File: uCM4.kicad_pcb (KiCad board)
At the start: 2 copper layers, 55 x 40 mm, 66 parts, among them J1 UART, J10 Conn_01x04, J11 Conn_02x06_Odd_Even, J2 Micro_SD_Card_Det, J3 I2C1, J4 USB_B_Micro, J5 DummyJ, J6 DummyJ, J7 SolderJumper_2_Open, J8 Camera 0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

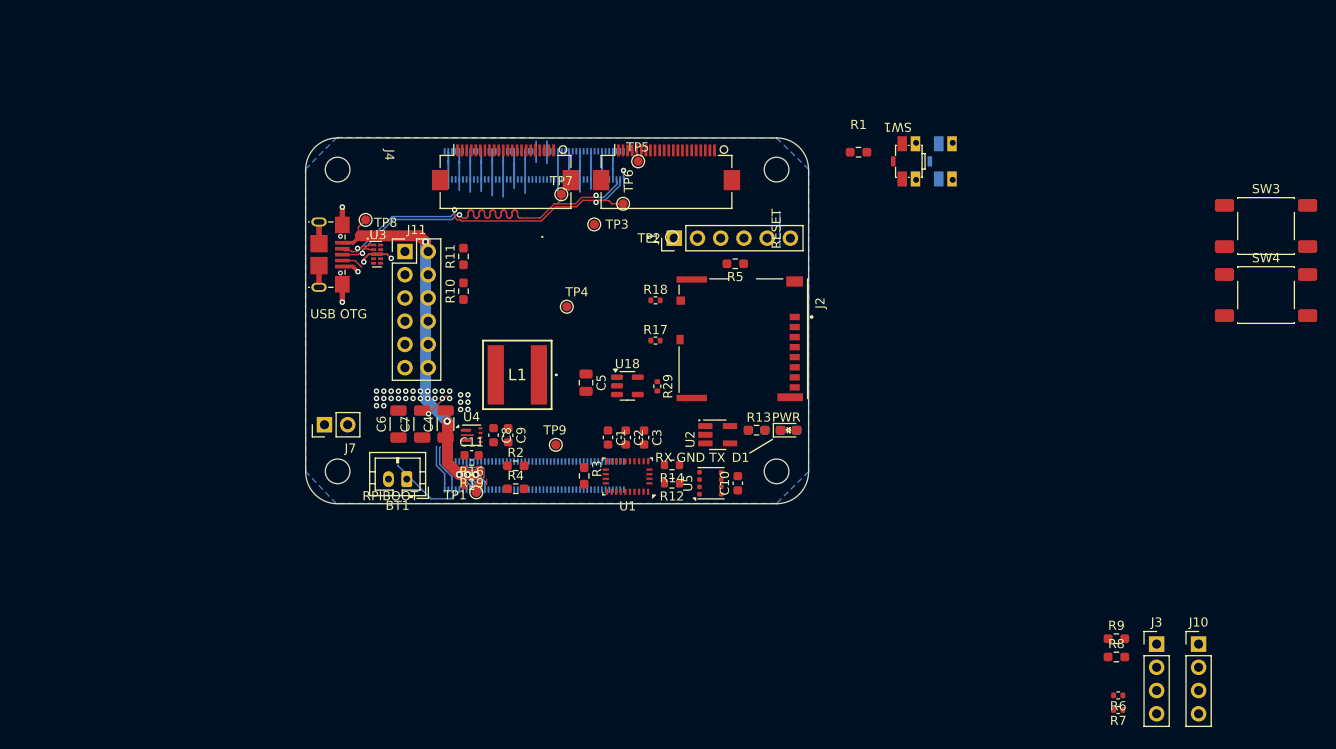
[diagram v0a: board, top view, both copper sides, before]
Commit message: Changing models & some initial routing
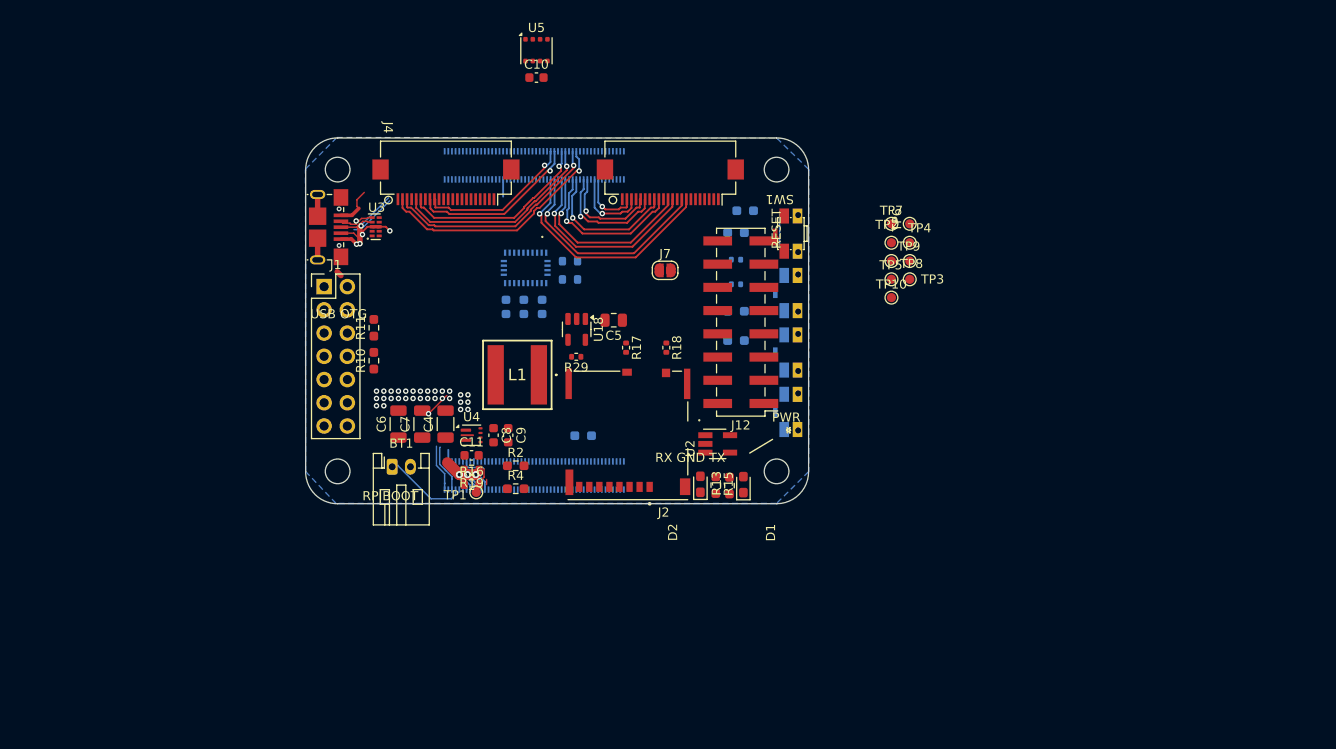
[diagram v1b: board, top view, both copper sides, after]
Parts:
- removed J10: Conn_01x04, Connector_PinHeader_2.54mm:PinHeader_1x04_P2.54mm_Vertical
- removed J11: Conn_02x06_Odd_Even, Connector_PinHeader_2.54mm:PinHeader_2x06_P2.54mm_Vertical
- removed J3: I2C1, Connector_PinHeader_2.54mm:PinHeader_1x04_P2.54mm_Vertical
- removed R5, R8, R9: 0, Resistor_SMD:R_0603_1608Metric_Pad0.98x0.95mm_HandSolder
- added J12: Conn_02x08_Odd_Even, Connector_PinHeader_2.54mm:PinHeader_2x08_P2.54mm_Vertical_SMD, F.Cu at (168.5, 105.2)
- added R20: 0, Resistor_SMD:R_0603_1608Metric_Pad0.98x0.95mm_HandSolder, B.Cu at (168.0, 107.2)
- added R21: 0, Resistor_SMD:R_0603_1608Metric_Pad0.98x0.95mm_HandSolder, B.Cu at (168.0, 95.4)
- added R22: 0, Resistor_SMD:R_0603_1608Metric_Pad0.98x0.95mm_HandSolder, B.Cu at (168.0, 104.0)
- added TP10: TestPoint, TestPoint:TestPoint_Pad_D1.0mm, F.Cu at (185.0, 102.5)
- BT1: footprint Connector_JST:JST_PH_B2B-PH-K_1x02_P2.00mm_Vertical -> Connector_JST:JST_PH_S2B-PH-K_1x02_P2.00mm_Horizontal
- C1, C2, C3, R1, R12, R14, R3, R6, R7, U1: moved to B.Cu
- D2, R15: moved to F.Cu
- J1: value UART -> Conn_02x07_Odd_Even; footprint Connector_PinHeader_2.54mm:PinHeader_1x06_P2.54mm_Vertical -> Connector_PinHeader_2.54mm:PinHeader_2x07_P2.54mm_Vertical
- J7: footprint Connector_PinHeader_2.54mm:PinHeader_1x02_P2.54mm_Vertical -> Jumper:SolderJumper-2_P1.3mm_Open_RoundedPad1.0x1.5mm
- SW3, SW4: footprint Button_Switch_SMD:SW_Push_1P1T_NO_E-Switch_TL3301NxxxxxG -> KiCAD_Randoms:PTS840_PM_SMTR_LFS; moved to B.Cu
- moved R6 63.4 mm to (168.0, 98.4), turned to 0 degrees
- moved R7 62.6 mm to (168.0, 101.0), turned to 0 degrees
- moved TP8 57.7 mm to (185.0, 98.5)
- moved SW3 55.8 mm to (174.0, 115.0), turned to -90 degrees
- moved SW4 52.0 mm to (174.0, 102.0), turned to -90 degrees
- moved U5 51.0 mm to (146.2, 75.4), turned to 0 degrees
- moved C10 49.5 mm to (146.2, 78.4), turned to 0 degrees
- moved TP9 43.6 mm to (187.0, 98.5)
- moved J7 40.9 mm to (160.2, 99.5), turned to 0 degrees
- moved J1 38.7 mm to (123.0, 101.3), turned to 0 degrees
- moved TP4 38.1 mm to (187.0, 96.5)
- moved TP7 36.2 mm to (185.0, 94.4)
- moved TP3 35.0 mm to (187.0, 100.5)
- moved TP5 30.6 mm to (185.0, 100.5)
- moved TP6 29.6 mm to (185.0, 96.5)
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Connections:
- net Net-(BT1-+) renamed /BAT_IN
- J1 pad 1: GND -> /GPS_EN_1
- J1 pad 2: /CTS0 -> /GPS_EN_2
- J1 pad 3: Net-(J1-Pin_3) -> GND
- J1 pad 4: /TXD0 -> GND
- J1 pad 5: /RXD0 -> /TXD3
- J1 pad 6: /RTS0 -> /TXD4
- R10 pad 1: Net-(J11-Pin_10) -> Net-(J1-Pin_10)
- R11 pad 2: Net-(J11-Pin_9) -> Net-(J1-Pin_9)
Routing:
- net GND: track 93.4 -> 19.5 mm, vias 21 -> 20
- net /USB_N: track 41.3 -> 4.07 mm, vias 3 -> 1
- net +5V: track 56.7 -> 24.2 mm, vias 5 -> 3
- net /USB_P: track 43.3 -> 14.2 mm, vias 3 -> 1
- net /CAM0_D0_N: track 0.00 -> 26.4 mm, vias 0 -> 1
- net /CAM1_D3_P: track 0.00 -> 25.9 mm, vias 0 -> 1
- net /CAM0_D0_P: track 0.00 -> 24.5 mm, vias 0 -> 1
- net /CAM1_D3_N: track 0.00 -> 24.2 mm, vias 0 -> 1
- net /CAM0_D1_N: track 0.00 -> 22.6 mm, vias 0 -> 1
- net /CAM1_D2_P: track 0.00 -> 21.9 mm, vias 0 -> 1
- net /CAM0_D1_P: track 0.00 -> 21.2 mm, vias 0 -> 1
- net /CAM1_D2_N: track 0.00 -> 20.3 mm, vias 0 -> 1
- net /CAM0_C_N: track 0.00 -> 18.7 mm, vias 0 -> 1
- net /CAM1_C_P: track 0.00 -> 17.6 mm, vias 0 -> 1
- net /CAM0_C_P: track 0.00 -> 17.2 mm, vias 0 -> 1
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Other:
- board text added: "#Do we need the USB"
- board text added: "Check GPS orientation. And pinout needs to change."
- board text added: "Removed keepout area. Assuming external antenna use only!"
- board text removed: "POWER"

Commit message: Rearrangements
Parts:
- removed C10: 100nF, Capacitor_SMD:C_0603_1608Metric
- removed R21, R22: 0, Resistor_SMD:R_0603_1608Metric_Pad0.98x0.95mm_HandSolder
- removed U5: BME690, Package_LGA:Bosch_LGA-8_3x3mm_P0.8mm_ClockwisePinNumbering
- added C13: 100nF, Capacitor_SMD:C_0603_1608Metric, F.Cu at (96.7, 110.5)
- added IC1: MAX17048G+, CM4:SON50P200X200X80-9N-D, F.Cu at (91.7, 111.0)
- added J10: USB_C_Receptacle, Connector_USB:USB_C_Receptacle_Amphenol_12401610E4-2A, F.Cu at (125.0, 97.1)
- added J11: SolderJumper_2_Open, Connector_PinHeader_2.54mm:PinHeader_1x02_P2.54mm_Vertical_SMD_Pin1Left, F.Cu at (105.4, 107.4)
- added J3: Conn_01x04, Connector_JST:JST_SH_BM03B-SRSS-TB_1x03-1MP_P1.00mm_Vertical, F.Cu at (92.5, 93.9)
- added R23: 0, Resistor_SMD:R_0603_1608Metric_Pad0.98x0.95mm_HandSolder, F.Cu at (96.8, 108.0)
- added R5: 0, Resistor_SMD:R_0603_1608Metric_Pad0.98x0.95mm_HandSolder, F.Cu at (96.8, 105.5)
- added R8: 5.1k, Resistor_SMD:R_0402_1005Metric, F.Cu at (110.8, 104.8)
- added R9: 5.1k, Resistor_SMD:R_0402_1005Metric, F.Cu at (110.8, 106.8)
- added U6: TP4057, Package_TO_SOT_SMD:TSOT-23-6, F.Cu at (92.1, 106.7)
- C1, C2, C3, R1, R12, R14, R20, R6, R7, U1: moved to F.Cu
- J1: footprint Connector_PinHeader_2.54mm:PinHeader_2x07_P2.54mm_Vertical -> Connector_PinHeader_2.54mm:PinHeader_2x07_P2.54mm_Vertical_SMD
- J4: value USB_B_Micro -> Conn_01x04; footprint Special:U254-05XX-4BH81 -> Connector_JST:JST_SH_BM03B-SRSS-TB_1x03-1MP_P1.00mm_Vertical
- J7: footprint Jumper:SolderJumper-2_P1.3mm_Open_RoundedPad1.0x1.5mm -> Connector_PinHeader_2.54mm:PinHeader_1x02_P2.54mm_Vertical_SMD_Pin1Left
- moved J4 28.2 mm to (97.5, 100.5), turned to 0 degrees
- moved J1 10.9 mm to (125.5, 111.9)
- moved R6 7.27 mm to (161.5, 101.7), turned to 180 degrees
- moved R7 7.21 mm to (161.4, 104.0)
- moved R20 6.84 mm to (161.3, 108.5)
- moved C3 5.18 mm to (146.8, 98.3), turned to -90 degrees
- moved C1 5.18 mm to (142.8, 98.3), turned to -90 degrees
- moved C2 5.18 mm to (144.8, 98.3), turned to -90 degrees
- moved R12 4.82 mm to (149.8, 103.3)
- moved R18 4.07 mm to (156.4, 108.8)
- moved U1 3.35 mm to (145.0, 102.6)
- moved R17 1.45 mm to (154.7, 108.7)
- moved R1 1.19 mm to (169.9, 93.8)
- moved R14 0.82 mm to (149.8, 101.3)
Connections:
- BT1 pad 1: /BAT_IN -> /BAT
- C8 pad 1: /BAT_IN -> /BOOST_IN
- C9 pad 1: /BAT_IN -> /BOOST_IN
- J12 pad 10: /SCL1 -> unconnected-(J12-Pin_10-Pad10)
- J12 pad 12: /SDA1 -> unconnected-(J12-Pin_12-Pad12)
- J12 pad 14: GND -> unconnected-(J12-Pin_14-Pad14)
- J12 pad 16: Net-(J12-Pin_16) -> unconnected-(J12-Pin_16-Pad16)
- J12 pad 2: /SCL0 -> unconnected-(J12-Pin_2-Pad2)
- J12 pad 4: /SDA0 -> unconnected-(J12-Pin_4-Pad4)
- J12 pad 6: GND -> unconnected-(J12-Pin_6-Pad6)
- J12 pad 8: Net-(J12-Pin_8) -> unconnected-(J12-Pin_8-Pad8)
- J4 pad 1: +5V -> GND
- J4 pad 2: /USB_N -> Net-(J4-Pin_2)
- J4 pad 3: /USB_P -> /SDA1
- L1 pad 1: /BAT_IN -> /BOOST_IN
- Module1 pad 101: /USB_ID -> Net-(J11-Pin_2)
- Module1 pad 41: unconnected-(Module1A-GPIO25-Pad41) -> /BAT_ALERT
- U4 pad 5: /BAT_IN -> /BOOST_IN
- U4 pad 7: /BAT_IN -> /BOOST_IN
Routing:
- net /USB_P: track 14.2 -> 0.00 mm, vias 1 -> 0
- net GND: track 19.5 -> 5.98 mm, vias 20 -> 16
- net +5V: track 24.2 -> 19.8 mm
- net /USB_N: track 4.07 -> 0.00 mm, vias 1 -> 0
- net /USB_ID: track 2.42 -> 0.00 mm
- net Net-(J1-Pin_10): vias 0 -> 2
- net /TXD4: vias 6 -> 5
- net /RXD3: vias 2 -> 1

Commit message: Changed some parts and hopeful final PCB arrangement.
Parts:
- removed J1: Conn_02x07_Odd_Even, Connector_PinHeader_2.54mm:PinHeader_2x07_P2.54mm_Vertical_SMD
- removed J3: Conn_01x04, Connector_JST:JST_SH_BM03B-SRSS-TB_1x03-1MP_P1.00mm_Vertical
- removed R11, R5: 0, Resistor_SMD:R_0603_1608Metric_Pad0.98x0.95mm_HandSolder
- removed SW4: SW_Push, KiCAD_Randoms:PTS840_PM_SMTR_LFS
- added D3: LED, LED_SMD:LED_0402_1005Metric, F.Cu at (160.1, 111.2)
- added D6: LED, LED_SMD:LED_0402_1005Metric, F.Cu at (147.1, 112.2)
- added D7: LED, LED_SMD:LED_0402_1005Metric, F.Cu at (141.3, 112.1)
- added D8: SS34, Diode_SMD:D_SMA, F.Cu at (135.4, 105.8)
- added J13: Conn_02x07_Odd_Even, Connector_PinHeader_2.54mm:PinHeader_2x07_P2.54mm_Vertical_SMD, F.Cu at (125.5, 101.2)
- added Q2: AO3401A, Package_TO_SOT_SMD:SOT-23, F.Cu at (131.5, 122.5)
- added R21: 100k, Resistor_SMD:R_0402_1005Metric, F.Cu at (135.3, 120.6)
- added R22: 2.4k, Resistor_SMD:R_0402_1005Metric, F.Cu at (147.2, 111.1)
- added R24: 1k, Resistor_SMD:R_0402_1005Metric, F.Cu at (147.2, 113.2)
- added TP11: TestPoint, TestPoint:TestPoint_Pad_D1.0mm, F.Cu at (134.0, 98.7)
- added TP12: TestPoint, TestPoint:TestPoint_Pad_D1.0mm, F.Cu at (134.0, 101.8)
- BT1: footprint Connector_JST:JST_PH_S2B-PH-K_1x02_P2.00mm_Horizontal -> CM4:JST_B2B-PH-SM4-TB
- J10: footprint Connector_USB:USB_C_Receptacle_Amphenol_12401610E4-2A -> Connector_USB:USB_C_Receptacle_GCT_USB4105-xx-A_16P_TopMnt_Horizontal
- J4: footprint Connector_JST:JST_SH_BM03B-SRSS-TB_1x03-1MP_P1.00mm_Vertical -> Connector_JST:JST_SH_BM04B-SRSS-TB_1x04-1MP_P1.00mm_Vertical
- R10: value 0 -> 1k
- R3, SW2, SW3: moved to F.Cu
- moved R23 77.0 mm to (171.5, 127.0)
- moved J4 71.9 mm to (166.2, 121.5), turned to 90 degrees
- moved J11 53.4 mm to (158.8, 105.5)
- moved U6 52.2 mm to (144.0, 112.2)
- moved TP2 49.4 mm to (137.7, 97.8), turned to 90 degrees
- moved IC1 48.4 mm to (135.6, 131.5), turned to 180 degrees
- moved TP7 47.6 mm to (137.7, 99.7), turned to 90 degrees
- moved TP4 47.3 mm to (139.8, 97.8), turned to 90 degrees
- moved TP6 45.4 mm to (139.8, 99.8), turned to 90 degrees
- moved TP9 45.3 mm to (141.8, 97.8), turned to 90 degrees
- moved TP3 43.3 mm to (143.8, 97.8), turned to 90 degrees
- moved TP8 43.3 mm to (141.8, 99.8), turned to 90 degrees
- moved C13 43.1 mm to (135.5, 129.3), turned to 180 degrees
- moved TP5 41.3 mm to (143.8, 99.8), turned to 90 degrees
- moved TP10 39.3 mm to (145.8, 99.8), turned to 90 degrees
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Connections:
- J12 pad 10: unconnected-(J12-Pin_10-Pad10) -> /SPI6_MISO
- J12 pad 11: /RTS0 -> /CTS0
- J12 pad 12: unconnected-(J12-Pin_12-Pad12) -> /SPI6_MOSI
- J12 pad 14: unconnected-(J12-Pin_14-Pad14) -> /SPI6_CE0_N
- J12 pad 16: unconnected-(J12-Pin_16-Pad16) -> /SPI6_CE1_N
- J12 pad 2: unconnected-(J12-Pin_2-Pad2) -> +5V
- J12 pad 3: /CTS0 -> /RTS0
- J12 pad 4: unconnected-(J12-Pin_4-Pad4) -> +3V3
- J12 pad 6: unconnected-(J12-Pin_6-Pad6) -> GND
- J12 pad 7: /TXD0 -> /RXD0
- J12 pad 8: unconnected-(J12-Pin_8-Pad8) -> /SPI6_SCLK
- J12 pad 9: /RXD0 -> /TXD0
- Module1 pad 24: unconnected-(Module1A-GPIO26-Pad24) -> /GPS_EXTINT
- Module1 pad 25: unconnected-(Module1A-GPIO21-Pad25) -> /SPI6_SCLK
- Module1 pad 26: unconnected-(Module1A-GPIO19-Pad26) -> /SPI6_MISO
- Module1 pad 27: unconnected-(Module1A-GPIO20-Pad27) -> /SPI6_MOSI
- Module1 pad 30: unconnected-(Module1A-GPIO6-Pad30) -> /GPS_TIME_1
- Module1 pad 38: unconnected-(Module1A-GPIO11-Pad38) -> /GPS_TIME_2
- Module1 pad 44: unconnected-(Module1A-GPIO10-Pad44) -> /GPS_READY
- Module1 pad 46: unconnected-(Module1A-GPIO22-Pad46) -> /GPIO22
- Module1 pad 47: /BTN1 -> unconnected-(Module1A-GPIO23-Pad47)
- Module1 pad 48: unconnected-(Module1A-GPIO27-Pad48) -> /SPI6_CE1_N
- Module1 pad 49: unconnected-(Module1A-GPIO18-Pad49) -> /SPI6_CE0_N
- R10 pad 1: Net-(J1-Pin_10) -> /GPIO22
- R10 pad 2: +5V -> Net-(D3-K)
- TP10 pad 1: /BAT_IN -> /BAT
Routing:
- net +5V: track 19.8 -> 0.00 mm, vias 3 -> 0
- net +1V8: track 5.44 -> 2.55 mm
- net GND: track 5.98 -> 3.15 mm, vias 16 -> 29
- net /SD_DAT2: track 0.55 -> 0.00 mm
- net Net-(J1-Pin_10): vias 2 -> 0
- net /TXD4: vias 5 -> 0
- net /TXD3: vias 7 -> 0
- net /RXD3: vias 1 -> 0
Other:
- board size 55 x 40 mm -> 55 x 48 mm

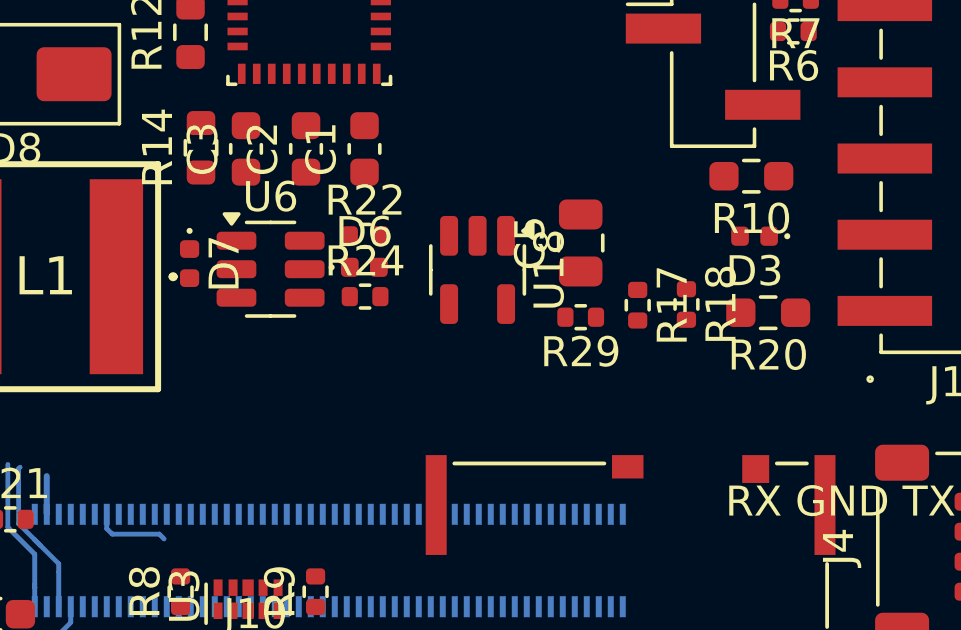
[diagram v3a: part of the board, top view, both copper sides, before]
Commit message: Moving LEDs
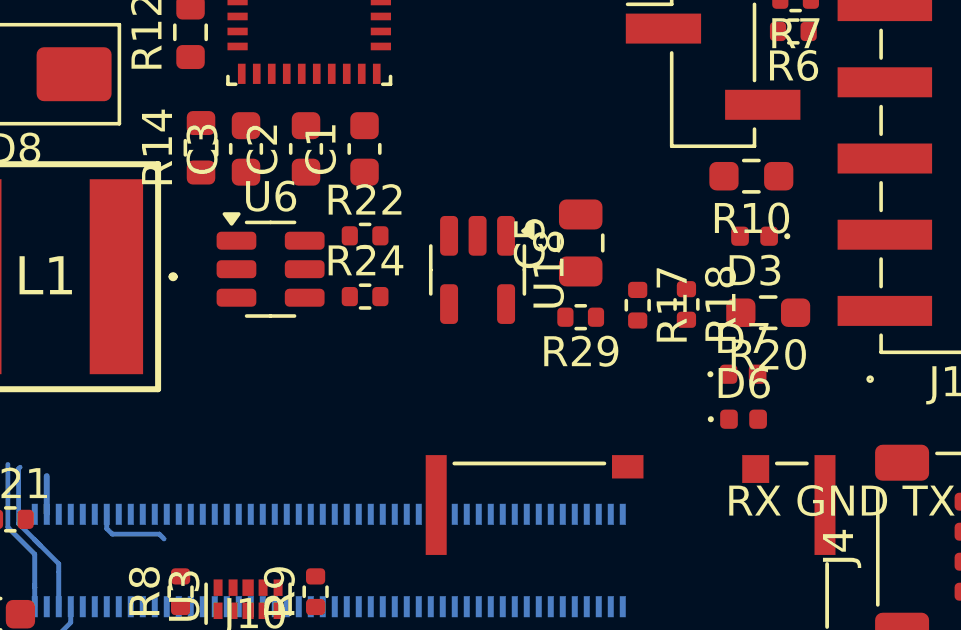
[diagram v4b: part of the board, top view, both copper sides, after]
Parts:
- moved D7 18.8 mm to (159.8, 115.8), turned to 0 degrees
- moved D6 13.6 mm to (159.8, 117.2)
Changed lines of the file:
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@@
 	(footprint "LED_SMD:LED_0402_1005Metric"
 		(layer "F.Cu")
-		(at 141.3 112.0625 -90)
+		(at 159.75 115.75)
 		(descr "LED SMD 0402 (1005 Metric), square (rectangular) end terminal, IPC-7351 nominal, (Body size source: http://www.tortai-tech.com/upload/download/2011102023233369053.pdf), generated with kicad-footprint-generator")
 		(tags "LED")
 		(property "Reference" "D7"
-			(at 0 -1.17 90)
+			(at 0 -1.17 0)
 			(layer "F.SilkS")
 			(effects
@@
 		)
 		(property "Value" "LED"
-			(at 0 1.17 90)
+			(at 0 1.17 0)
 			(layer "F.Fab")
 			(effects
@@
 		)
 		(property "Datasheet" "~"
-			(at 0 0 90)
+			(at 0 0 0)
 			(layer "F.Fab")
 			(hide yes)
@@
 		)
 		(property "Description" "Light emitting diode"
-			(at 0 0 90)
+			(at 0 0 0)
 			(layer "F.Fab")
 			(hide yes)
@@
 		)
 		(property "Sim.Pins" "1=K 2=A"
-			(at 0 0 270)
+			(at 0 0 0)
 			(unlocked yes)
 			(layer "F.Fab")
@@
 		(fp_circle
 			(center -1.089999 -0.000001)
-			(end -1.040002 -0.000004)
+			(end -1.040001 -0.000004)
 			(stroke
 				(width 0.1)
@@
 		)
 		(fp_line
-			(start -0.930001 0.470002)
-			(end -0.93 -0.470001)
+			(start -0.930002 0.470002)
+			(end -0.93 -0.47)
 			(stroke
 				(width 0.05)
@@
 		)
 		(fp_line
-			(start 0.93 0.470001)
-			(end -0.930001 0.470002)
+			(start -0.93 -0.47)
+			(end 0.930002 -0.470002)
 			(stroke
 				(width 0.05)
@@
 		)
 		(fp_line
-			(start -0.93 -0.470001)
-			(end 0.930001 -0.470002)
+			(start 0.93 0.47)
+			(end -0.930002 0.470002)
 			(stroke
 				(width 0.05)
@@
 		)
 		(fp_line
-			(start 0.930001 -0.470002)
-			(end 0.93 0.470001)
+			(start 0.930002 -0.470002)
+			(end 0.93 0.47)
 			(stroke
 				(width 0.05)
@@
 		)
 		(fp_line
-			(start -0.5 0.25)
-			(end -0.5 -0.25)
+			(start -0.5 -0.25)
+			(end 0.5 -0.25)
 			(stroke
 				(width 0.1)
@@
 		)
 		(fp_line
-			(start 0.5 0.25)
-			(end -0.5 0.25)
+			(start -0.5 0.25)
+			(end -0.5 -0.25)
 			(stroke
 				(width 0.1)
@@
 		)
 		(fp_line
-			(start -0.399998 0.249999)
-			(end -0.399999 -0.249998)
+			(start -0.399999 0.25)
+			(end -0.4 -0.249999)
 			(stroke
 				(width 0.1)
@@
 		)
 		(fp_line
-			(start -0.5 -0.25)
-			(end 0.5 -0.25)
+			(start 0.5 -0.25)
+			(end 0.5 0.25)
 			(stroke
 				(width 0.1)
@@
 		)
 		(fp_line
-			(start 0.5 -0.25)
-			(end 0.5 0.25)
+			(start 0.5 0.25)
+			(end -0.5 0.25)
 			(stroke
 				(width 0.1)
@@
 		)
 		(fp_text user "${REFERENCE}"
-			(at 0 0 90)
+			(at 0 0 0)
 			(layer "F.Fab")
 			(effects
@@
 		)
 		(pad "1" smd roundrect
-			(at -0.484998 0 270)
+			(at -0.484998 0)
 			(size 0.59 0.64)
 			(layers "F.Cu" "F.Mask" "F.Paste")
@@
 		)
 		(pad "2" smd roundrect
-			(at 0.484998 0 270)
+			(at 0.484998 0)
 			(size 0.59 0.64)
 			(layers "F.Cu" "F.Mask" "F.Paste")
@@
 	(footprint "LED_SMD:LED_0402_1005Metric"
 		(layer "F.Cu")
-		(at 147.125 112.1875)
+		(at 159.765 117.25)
 		(descr "LED SMD 0402 (1005 Metric), square (rectangular) end terminal, IPC-7351 nominal, (Body size source: http://www.tortai-tech.com/upload/download/2011102023233369053.pdf), generated with kicad-footprint-generator")
 		(tags "LED")
